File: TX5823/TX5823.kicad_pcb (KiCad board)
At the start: 4 copper layers, 50 x 50 mm, 96 parts, among them IC1 ATMEGA328P-A, IC2 ATTINY13A-SS, P1 Akku_in, P2 ISP, P3 Mavlink, P4 CONN_01X01, P5 CONN_01X01, P6 CONN_01X01, P7 CONN_01X01, Q1 MOSFET_P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

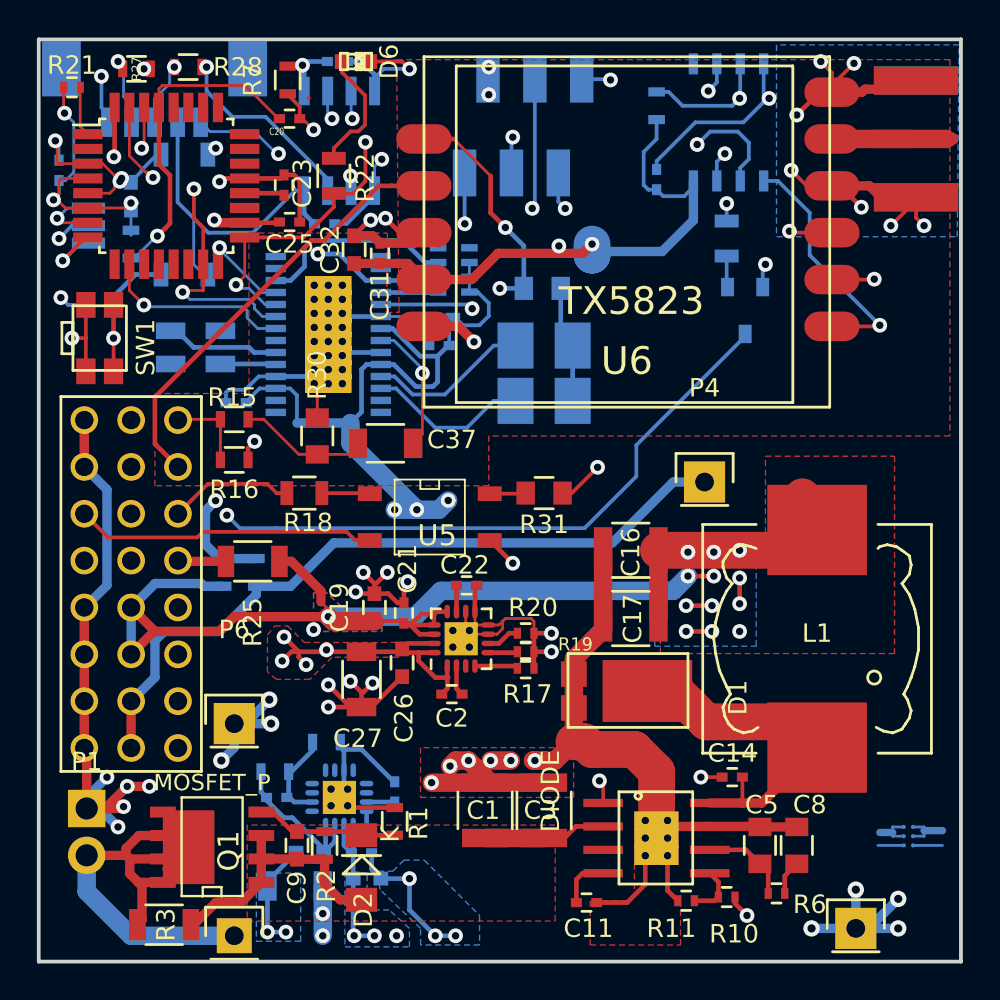
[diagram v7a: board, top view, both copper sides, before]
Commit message: 5V Anbindung Atmel verbessert Bestückungsdruck hinzugefügt
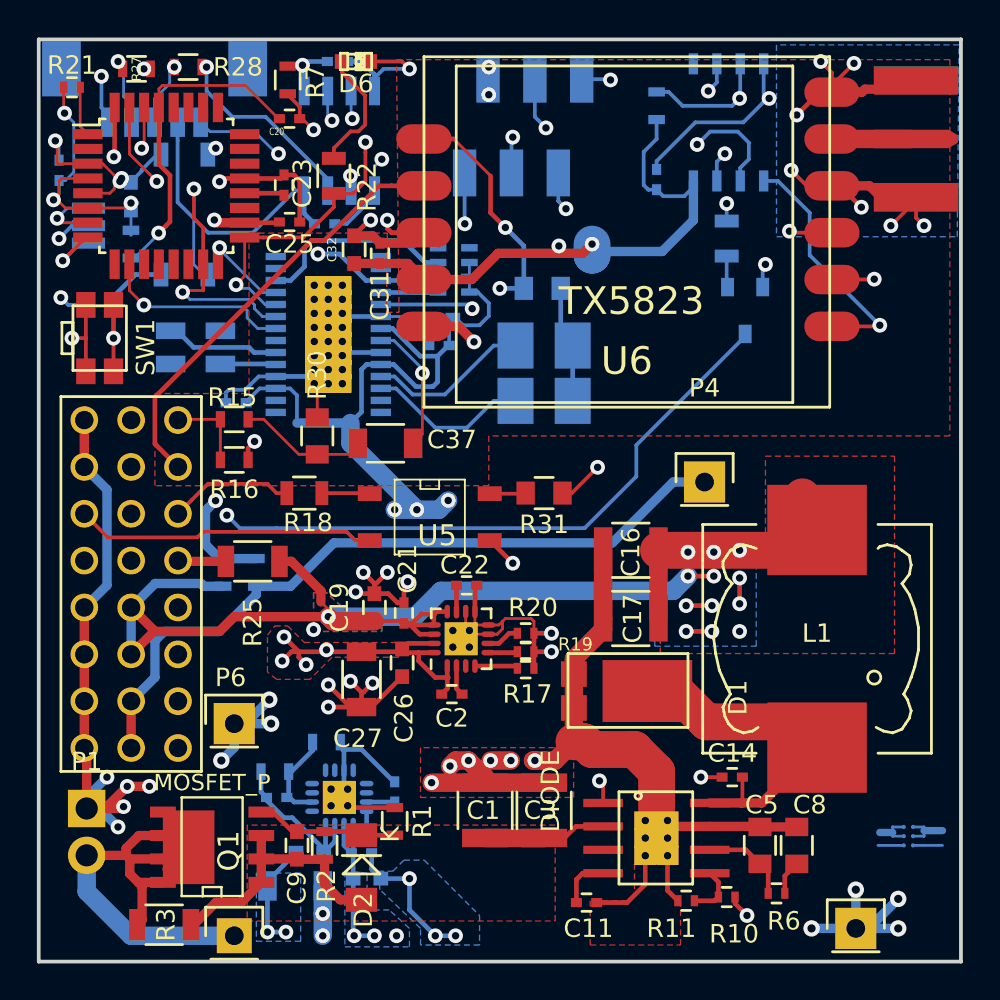
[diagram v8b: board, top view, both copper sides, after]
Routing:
- net /MOSI: track 39.5 -> 37.0 mm
- net +5V: track 189.6 -> 188.5 mm
